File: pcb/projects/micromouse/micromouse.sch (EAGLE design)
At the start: 52 parts, among them M1 332-06, M2 332-06, U1 DSPIC33FJ64MC804-H/PT, U2 UA78M33CKCS, U3 UA78M05CKCS

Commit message: Most wiring done
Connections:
- net BUTTON: now also U1.AN7/DAC1LM/RP17/CN9/RC1; no longer U1.SOSCO/T1CK/CN0/RA4
- net DSENS2: now also U1.AN6/DAC1RM/RP16/CN8/RC0; no longer U1.AN5/C1IN+/RP3/CN7/RB3
- net DSENS3: now also U1.AN5/C1IN+/RP3/CN7/RB3; no longer U1.AN6/DAC1RM/RP16/CN8/RC0
- net M1_D1: now also U1.RP21/CN26/PMA3/RC5; no longer U1.SDA1/RP9/CN21/PMD3/RB9
- net M1_D2: now also U1.RP20/CN25/PMA4/RC4; no longer U1.PWM2H1/RP22/CN18/PMA1/RC6
- net M1_EA: now also U1.TDI/PMA9/RA9; no longer U1.RP24/CN20/PMA5/RC8
- net M1_EB: now also U1.RP19/CN28/PMBE/RC3; no longer U1.PWM2L1/RP23/CN17/PMA0/RC7
- net M2_D1: now also U1.PWM2H1/RP22/CN18/PMA1/RC6; no longer U1.RP21/CN26/PMA3/RC5
- net M2_D2: now also U1.SDA1/RP9/CN21/PMD3/RB9; no longer U1.RP20/CN25/PMA4/RC4
- net M2_EA: now also U1.RP24/CN20/PMA5/RC8; no longer U1.TDI/PMA9/RA9
- net M2_EB: now also U1.PWM2L1/RP23/CN17/PMA0/RC7; no longer U1.RP19/CN28/PMBE/RC3
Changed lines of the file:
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@@
 </segment>
 <segment>
-<pinref part="U1" gate="A" pin="PWM2L1/RP23/CN17/PMA0/RC7"/>
-<wire x1="91.44" y1="154.94" x2="116.84" y2="154.94" width="0.1524" layer="91"/>
-<label x="91.44" y="154.94" size="1.778" layer="95"/>
+<pinref part="U1" gate="A" pin="RP19/CN28/PMBE/RC3"/>
+<wire x1="322.58" y1="139.7" x2="299.72" y2="139.7" width="0.1524" layer="91"/>
+<label x="314.96" y="139.7" size="1.778" layer="95"/>
 </segment>
 </net>
@@
 </segment>
 <segment>
-<pinref part="U1" gate="A" pin="RP24/CN20/PMA5/RC8"/>
-<wire x1="91.44" y1="152.4" x2="116.84" y2="152.4" width="0.1524" layer="91"/>
-<label x="91.44" y="152.4" size="1.778" layer="95"/>
+<pinref part="U1" gate="A" pin="TDI/PMA9/RA9"/>
+<wire x1="322.58" y1="137.16" x2="299.72" y2="137.16" width="0.1524" layer="91"/>
+<label x="314.96" y="137.16" size="1.778" layer="95"/>
 </segment>
 </net>
@@
 </segment>
 <segment>
-<pinref part="U1" gate="A" pin="SDA1/RP9/CN21/PMD3/RB9"/>
-<wire x1="91.44" y1="160.02" x2="116.84" y2="160.02" width="0.1524" layer="91"/>
-<label x="91.44" y="160.02" size="1.778" layer="95"/>
+<pinref part="U1" gate="A" pin="RP21/CN26/PMA3/RC5"/>
+<wire x1="322.58" y1="144.78" x2="299.72" y2="144.78" width="0.1524" layer="91"/>
+<label x="314.96" y="144.78" size="1.778" layer="95"/>
 </segment>
 </net>
@@
 </segment>
 <segment>
-<pinref part="U1" gate="A" pin="PWM2H1/RP22/CN18/PMA1/RC6"/>
-<wire x1="91.44" y1="157.48" x2="116.84" y2="157.48" width="0.1524" layer="91"/>
-<label x="91.44" y="157.48" size="1.778" layer="95"/>
+<pinref part="U1" gate="A" pin="RP20/CN25/PMA4/RC4"/>
+<wire x1="322.58" y1="142.24" x2="299.72" y2="142.24" width="0.1524" layer="91"/>
+<label x="314.96" y="142.24" size="1.778" layer="95"/>
 </segment>
 </net>
@@
 </segment>
 <segment>
-<pinref part="U1" gate="A" pin="RP19/CN28/PMBE/RC3"/>
-<wire x1="322.58" y1="139.7" x2="299.72" y2="139.7" width="0.1524" layer="91"/>
-<label x="314.96" y="139.7" size="1.778" layer="95"/>
+<pinref part="U1" gate="A" pin="PWM2L1/RP23/CN17/PMA0/RC7"/>
+<wire x1="91.44" y1="154.94" x2="116.84" y2="154.94" width="0.1524" layer="91"/>
+<label x="91.44" y="154.94" size="1.778" layer="95"/>
 </segment>
 </net>
@@
 </segment>
 <segment>
-<pinref part="U1" gate="A" pin="TDI/PMA9/RA9"/>
-<wire x1="322.58" y1="137.16" x2="299.72" y2="137.16" width="0.1524" layer="91"/>
-<label x="314.96" y="137.16" size="1.778" layer="95"/>
+<pinref part="U1" gate="A" pin="RP24/CN20/PMA5/RC8"/>
+<wire x1="91.44" y1="152.4" x2="116.84" y2="152.4" width="0.1524" layer="91"/>
+<label x="91.44" y="152.4" size="1.778" layer="95"/>
 </segment>
 </net>
@@
 </segment>
 <segment>
-<pinref part="U1" gate="A" pin="RP21/CN26/PMA3/RC5"/>
-<wire x1="322.58" y1="144.78" x2="299.72" y2="144.78" width="0.1524" layer="91"/>
-<label x="314.96" y="144.78" size="1.778" layer="95"/>
+<pinref part="U1" gate="A" pin="PWM2H1/RP22/CN18/PMA1/RC6"/>
+<wire x1="91.44" y1="157.48" x2="116.84" y2="157.48" width="0.1524" layer="91"/>
+<label x="91.44" y="157.48" size="1.778" layer="95"/>
 </segment>
 </net>
@@
 </segment>
 <segment>
-<pinref part="U1" gate="A" pin="RP20/CN25/PMA4/RC4"/>
-<wire x1="322.58" y1="142.24" x2="299.72" y2="142.24" width="0.1524" layer="91"/>
-<label x="314.96" y="142.24" size="1.778" layer="95"/>
+<pinref part="U1" gate="A" pin="SDA1/RP9/CN21/PMD3/RB9"/>
+<wire x1="91.44" y1="160.02" x2="116.84" y2="160.02" width="0.1524" layer="91"/>
+<label x="91.44" y="160.02" size="1.778" layer="95"/>
 </segment>
 </net>
@@
 </segment>
 <segment>
+<pinref part="U1" gate="A" pin="AN6/DAC1RM/RP16/CN8/RC0"/>
+<wire x1="320.04" y1="111.76" x2="299.72" y2="111.76" width="0.1524" layer="91"/>
+<label x="309.88" y="111.76" size="1.778" layer="95"/>
+</segment>
+</net>
+<net name="DSENS3" class="0">
+<segment>
+<wire x1="86.36" y1="195.58" x2="60.96" y2="195.58" width="0.1524" layer="91"/>
+<label x="76.2" y="195.58" size="1.778" layer="95"/>
+<pinref part="DIST3S" gate="1" pin="P"/>
+</segment>
+<segment>
 <pinref part="U1" gate="A" pin="AN5/C1IN+/RP3/CN7/RB3"/>
 <wire x1="320.04" y1="109.22" x2="299.72" y2="109.22" width="0.1524" layer="91"/>
 <label x="309.88" y="109.22" size="1.778" layer="95"/>
-</segment>
-</net>
-<net name="DSENS3" class="0">
-<segment>
-<wire x1="86.36" y1="195.58" x2="60.96" y2="195.58" width="0.1524" layer="91"/>
-<label x="76.2" y="195.58" size="1.778" layer="95"/>
-<pinref part="DIST3S" gate="1" pin="P"/>
-</segment>
-<segment>
-<pinref part="U1" gate="A" pin="AN6/DAC1RM/RP16/CN8/RC0"/>
-<wire x1="320.04" y1="111.76" x2="299.72" y2="111.76" width="0.1524" layer="91"/>
-<label x="309.88" y="111.76" size="1.778" layer="95"/>
 </segment>
 </net>
@@
 </segment>
 <segment>
-<pinref part="U1" gate="A" pin="SOSCO/T1CK/CN0/RA4"/>
-<wire x1="322.58" y1="134.62" x2="299.72" y2="134.62" width="0.1524" layer="91"/>
-<label x="314.96" y="134.62" size="1.778" layer="95"/>
-</segment>
-</net>
+<pinref part="U1" gate="A" pin="AN7/DAC1LM/RP17/CN9/RC1"/>
+<wire x1="320.04" y1="114.3" x2="299.72" y2="114.3" width="0.1524" layer="91"/>
+<label x="309.88" y="114.3" size="1.778" layer="95"/>
+</segment>
+</net>

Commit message: Complete wiring
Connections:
- net M1_D1: now also U1.RP20/CN25/PMA4/RC4; no longer U1.RP21/CN26/PMA3/RC5
- net M1_D2: now also U1.RP21/CN26/PMA3/RC5; no longer U1.RP20/CN25/PMA4/RC4
- net M1_EA: now also U1.RP19/CN28/PMBE/RC3; no longer U1.TDI/PMA9/RA9
- net M1_EB: now also U1.TDI/PMA9/RA9; no longer U1.RP19/CN28/PMBE/RC3
- net M1_PWM: now also U1.PWM1H2/DAC1RP/RP12/CN14/PMD0/RB12; no longer U1.PWM1H1/DAC1LP/RTCC/RP14/CN12/PMWR/RB14
- net M2_PWM: now also U1.PWM1H1/DAC1LP/RTCC/RP14/CN12/PMWR/RB14; no longer U1.PWM1H2/DAC1RP/RP12/CN14/PMD0/RB12
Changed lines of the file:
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@@
 </segment>
 <segment>
-<pinref part="U1" gate="A" pin="RP19/CN28/PMBE/RC3"/>
-<wire x1="322.58" y1="139.7" x2="299.72" y2="139.7" width="0.1524" layer="91"/>
-<label x="314.96" y="139.7" size="1.778" layer="95"/>
+<pinref part="U1" gate="A" pin="TDI/PMA9/RA9"/>
+<wire x1="322.58" y1="137.16" x2="299.72" y2="137.16" width="0.1524" layer="91"/>
+<label x="314.96" y="137.16" size="1.778" layer="95"/>
 </segment>
 </net>
@@
 </segment>
 <segment>
-<pinref part="U1" gate="A" pin="TDI/PMA9/RA9"/>
-<wire x1="322.58" y1="137.16" x2="299.72" y2="137.16" width="0.1524" layer="91"/>
-<label x="314.96" y="137.16" size="1.778" layer="95"/>
+<pinref part="U1" gate="A" pin="RP19/CN28/PMBE/RC3"/>
+<wire x1="322.58" y1="139.7" x2="299.72" y2="139.7" width="0.1524" layer="91"/>
+<label x="314.96" y="139.7" size="1.778" layer="95"/>
 </segment>
 </net>
@@
 </segment>
 <segment>
-<pinref part="U1" gate="A" pin="RP21/CN26/PMA3/RC5"/>
-<wire x1="322.58" y1="144.78" x2="299.72" y2="144.78" width="0.1524" layer="91"/>
-<label x="314.96" y="144.78" size="1.778" layer="95"/>
+<pinref part="U1" gate="A" pin="RP20/CN25/PMA4/RC4"/>
+<wire x1="322.58" y1="142.24" x2="299.72" y2="142.24" width="0.1524" layer="91"/>
+<label x="314.96" y="142.24" size="1.778" layer="95"/>
 </segment>
 </net>
@@
 </segment>
 <segment>
-<pinref part="U1" gate="A" pin="RP20/CN25/PMA4/RC4"/>
-<wire x1="322.58" y1="142.24" x2="299.72" y2="142.24" width="0.1524" layer="91"/>
-<label x="314.96" y="142.24" size="1.778" layer="95"/>
+<pinref part="U1" gate="A" pin="RP21/CN26/PMA3/RC5"/>
+<wire x1="322.58" y1="144.78" x2="299.72" y2="144.78" width="0.1524" layer="91"/>
+<label x="314.96" y="144.78" size="1.778" layer="95"/>
 </segment>
 </net>
@@
 </segment>
 <segment>
-<pinref part="U1" gate="A" pin="PWM1H1/DAC1LP/RTCC/RP14/CN12/PMWR/RB14"/>
-<wire x1="86.36" y1="127" x2="116.84" y2="127" width="0.1524" layer="91"/>
-<label x="86.36" y="127" size="1.778" layer="95"/>
+<pinref part="U1" gate="A" pin="PWM1H2/DAC1RP/RP12/CN14/PMD0/RB12"/>
+<wire x1="116.84" y1="137.16" x2="86.36" y2="137.16" width="0.1524" layer="91"/>
+<label x="86.36" y="137.16" size="1.778" layer="95"/>
 </segment>
 </net>
@@
 </segment>
 <segment>
-<pinref part="U1" gate="A" pin="PWM1H2/DAC1RP/RP12/CN14/PMD0/RB12"/>
-<wire x1="116.84" y1="137.16" x2="86.36" y2="137.16" width="0.1524" layer="91"/>
-<label x="86.36" y="137.16" size="1.778" layer="95"/>
+<pinref part="U1" gate="A" pin="PWM1H1/DAC1LP/RTCC/RP14/CN12/PMWR/RB14"/>
+<wire x1="86.36" y1="127" x2="116.84" y2="127" width="0.1524" layer="91"/>
+<label x="86.36" y="127" size="1.778" layer="95"/>
 </segment>
 </net>

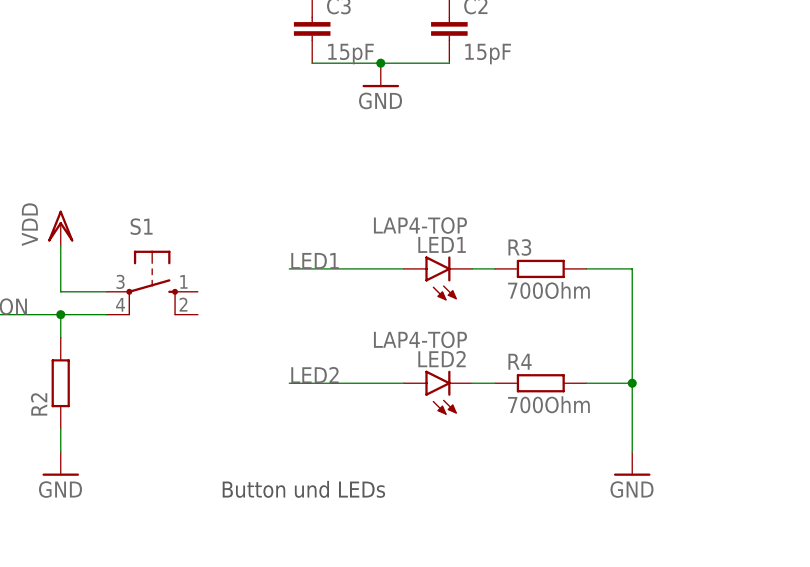
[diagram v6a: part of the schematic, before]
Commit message: Replace LED with 0805 package
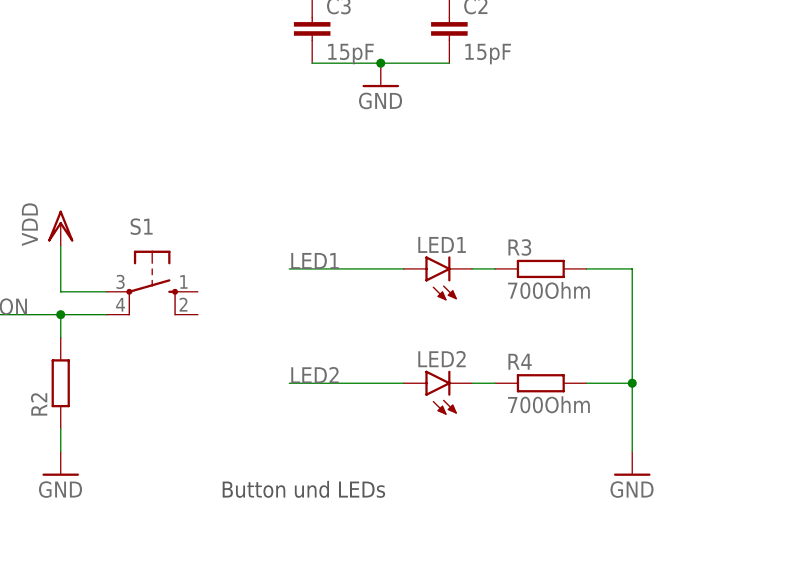
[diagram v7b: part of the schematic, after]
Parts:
- LED1, LED2: value LAP4-TOP -> (none); device led:LAP4-TOP -> led:LEDCHIP-LED0805
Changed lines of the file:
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@@
 <part name="GND19" library="supply1" library_urn="urn:adsk.eagle:library:371" deviceset="GND" device=""/>
 <part name="R2" library="rcl" library_urn="urn:adsk.eagle:library:334" deviceset="R-EU_" device="R0805" package3d_urn="urn:adsk.eagle:package:23553/2"/>
-<part name="LED1" library="led" library_urn="urn:adsk.eagle:library:259" deviceset="*P4" device="-TOP" package3d_urn="urn:adsk.eagle:package:15879/1" technology="LA"/>
-<part name="LED2" library="led" library_urn="urn:adsk.eagle:library:259" deviceset="*P4" device="-TOP" package3d_urn="urn:adsk.eagle:package:15879/1" technology="LA"/>
+<part name="LED1" library="led" library_urn="urn:adsk.eagle:library:259" deviceset="LED" device="CHIP-LED0805" package3d_urn="urn:adsk.eagle:package:15818/2"/>
+<part name="LED2" library="led" library_urn="urn:adsk.eagle:library:259" deviceset="LED" device="CHIP-LED0805" package3d_urn="urn:adsk.eagle:package:15818/2"/>
 <part name="R3" library="rcl" library_urn="urn:adsk.eagle:library:334" deviceset="R-EU_" device="R0805" package3d_urn="urn:adsk.eagle:package:23553/2" value="700Ohm"/>
 <part name="R4" library="rcl" library_urn="urn:adsk.eagle:library:334" deviceset="R-EU_" device="R0805" package3d_urn="urn:adsk.eagle:package:23553/2" value="700Ohm"/>

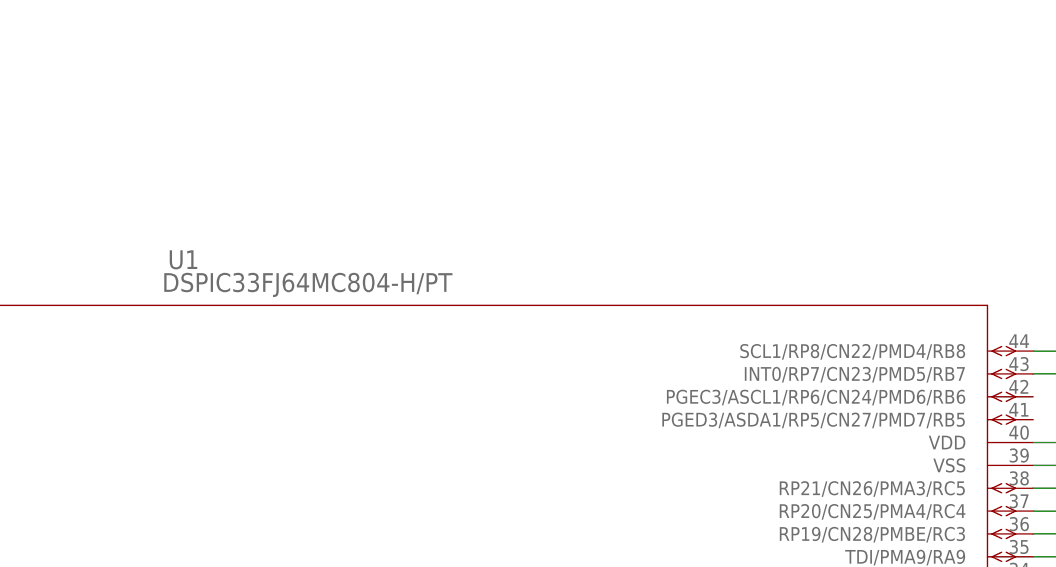
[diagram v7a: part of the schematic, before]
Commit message: Remove restricted areas for microship
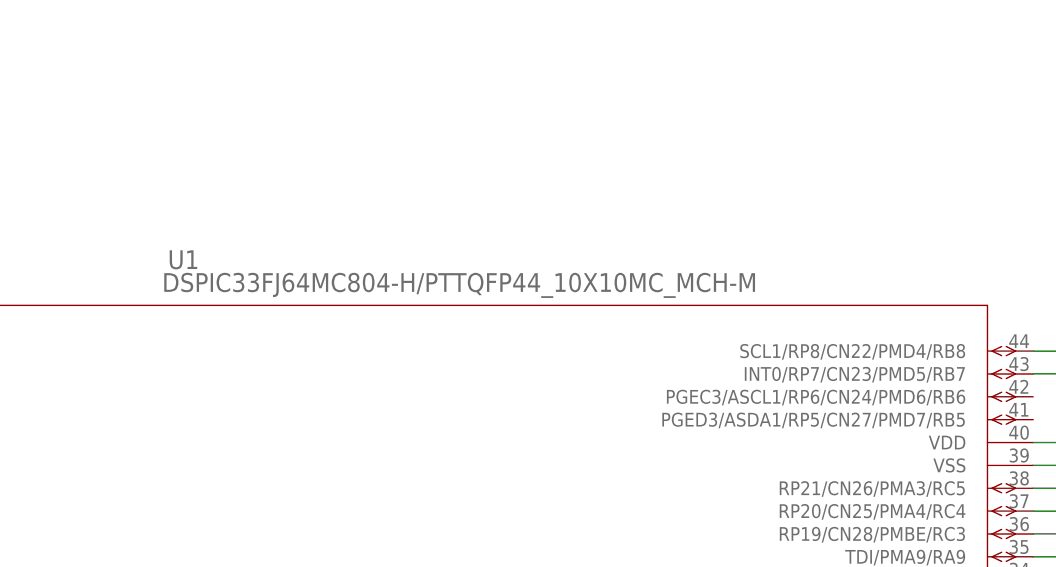
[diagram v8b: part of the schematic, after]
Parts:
- U1: value DSPIC33FJ64MC804-H/PT -> DSPIC33FJ64MC804-H/PTTQFP44_10X10MC_MCH-M; device micromouse:DSPIC33FJ64MC804-H/PT -> micromouse:DSPIC33FJ64MC804-H/PTTQFP44_10X10MC_MCH-M
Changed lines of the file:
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@@
 <part name="VDD8" library="supply1" library_urn="urn:adsk.eagle:library:371" deviceset="VDD" device=""/>
 <part name="VDD10" library="supply1" library_urn="urn:adsk.eagle:library:371" deviceset="VDD" device=""/>
-<part name="U1" library="micromouse" deviceset="DSPIC33FJ64MC804-H/PT" device=""/>
+<part name="U1" library="micromouse" deviceset="DSPIC33FJ64MC804-H/PT" device="TQFP44_10X10MC_MCH-M" value="DSPIC33FJ64MC804-H/PTTQFP44_10X10MC_MCH-M"/>
 <part name="Q1" library="crystal" library_urn="urn:adsk.eagle:library:204" deviceset="CRYSTAL" device="HC49S" package3d_urn="urn:adsk.eagle:package:12071/1"/>
 <part name="C2" library="rcl" library_urn="urn:adsk.eagle:library:334" deviceset="C-EU" device="C0805" package3d_urn="urn:adsk.eagle:package:23617/2" value="15pF"/>
